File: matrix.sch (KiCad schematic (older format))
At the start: 134 parts, among them K0:0 KEYSW, K0:1 KEYSW, K0:2 KEYSW, K0:3 KEYSW, K0:4 KEYSW, K10:0 KEYSW, K10:1 KEYSW, K10:2 KEYSW, K10:3 KEYSW, K10:4 KEYSW, K11:0 KEYSW, K11:1 KEYSW, K11:2 KEYSW, K11:3 KEYSW, K11:4 KEYSW, K12:0 KEYSW, K12:1 KEYSW, K12:2 KEYSW, K12:3 KEYSW, K12:4 KEYSW, K13:0 KEYSW, K13:1 KEYSW, K13:2 KEYSW, K13:3 KEYSW, K13:4 KEYSW, K1:0 KEYSW, K1:1 KEYSW, K1:2 KEYSW, K1:3 KEYSW, K1:4 KEYSW, K2:0 KEYSW, K2:1 KEYSW, K2:2 KEYSW, K2:3 KEYSW, K2:4 KEYSW, K3:0 KEYSW, K3:1 KEYSW, K3:2 KEYSW, K3:3 KEYSW, K3:4 KEYSW, K4:0 KEYSW, K4:1 KEYSW, K4:2 KEYSW, K4:3 KEYSW, K4:4 KEYSW, K5:0 KEYSW, K5:1 KEYSW, K5:2 KEYSW, K5:3 KEYSW, K5:4 KEYSW, K6:0 KEYSW, K6:1 KEYSW, K6:3 KEYSW, K7:0 KEYSW, K7:1 KEYSW, K7:3 KEYSW, K7:4 KEYSW, K8:0 KEYSW, K8:1 KEYSW, K8:2 KEYSW, K8:3 KEYSW, K8:4 KEYSW, K9:0 KEYSW, K9:1 KEYSW, K9:2 KEYSW, K9:3 KEYSW, K9:4 KEYSW

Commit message: Associate components and footprints
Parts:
- D0:0, D0:1, D0:2, D0:3, D0:4, D10:0, D10:1, D10:2, D10:3, D10:4, D11:0, D11:1, D11:2, D11:3, D11:4, D12:0, D12:1, D12:2, D12:3, D12:4, D13:0, D13:1, D13:2, D13:3, D13:4, D1:0, D1:1, D1:2, D1:3, D1:4, D2:0, D2:1, D2:2, D2:3, D2:4, D3:0, D3:1, D3:2, D3:3, D3:4, D4:0, D4:1, D4:2, D4:3, D4:4, D5:0, D5:1, D5:2, D5:3, D5:4, D6:0, D6:1, D6:3, D7:0, D7:1, D7:3, D7:4, D8:0, D8:1, D8:2, D8:3, D8:4, D9:0, D9:1, D9:2, D9:3, D9:4: footprint (none) -> keyboard_parts:D_SOD123_axial
- K0:0, K0:1, K0:2, K0:3, K0:4, K13:0, K13:1, K13:2, K13:3, K13:4, K6:1, K6:3, K7:1, K7:3: footprint (none) -> keebs:Mx_Alps_150
- K10:0, K10:1, K10:2, K10:3, K10:4, K11:0, K11:1, K11:2, K11:3, K11:4, K12:0, K12:1, K12:2, K12:3, K12:4, K1:0, K1:1, K1:2, K1:3, K1:4, K2:0, K2:1, K2:2, K2:3, K2:4, K3:0, K3:1, K3:2, K3:3, K3:4, K4:0, K4:1, K4:2, K4:3, K4:4, K5:0, K5:1, K5:2, K5:3, K6:0, K7:0, K7:4, K8:0, K8:1, K8:2, K8:3, K8:4, K9:0, K9:1, K9:2, K9:3, K9:4: footprint (none) -> keebs:Mx_Alps_100
- K5:4: footprint (none) -> keebs:Mx_Alps_200

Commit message: Revert "Temp #2"
This reverts commit d15dc5ae93d42b7242c0dbe6693181fd858ed452.
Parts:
- D6:1, D6:3, D7:1, D7:3: footprint keyboard_parts:D_SOD123_axial -> keyboard_parts:Mx_Alps_150_VERT
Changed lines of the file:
@@
 F 0 "D6:1" V 4800 3400 60  0000 C CNN
 F 1 "D" V 5100 3400 60  0001 C CNN
-F 2 "keyboard_parts:D_SOD123_axial" H 4950 3450 60  0001 C CNN
+F 2 "keyboard_parts:Mx_Alps_150_VERT" H 4950 3450 60  0001 C CNN
 F 3 "" H 4950 3450 60  0000 C CNN
 	1    4950 3450
@@
 F 0 "D6:3" V 4800 4700 60  0000 C CNN
 F 1 "D" V 5100 4700 60  0001 C CNN
-F 2 "keyboard_parts:D_SOD123_axial" H 4950 4750 60  0001 C CNN
+F 2 "keyboard_parts:Mx_Alps_150_VERT" H 4950 4750 60  0001 C CNN
 F 3 "" H 4950 4750 60  0000 C CNN
 	1    4950 4750
@@
 F 0 "D7:1" V 5850 3400 60  0000 C CNN
 F 1 "D" V 6150 3400 60  0001 C CNN
-F 2 "keyboard_parts:D_SOD123_axial" H 6000 3450 60  0001 C CNN
+F 2 "keyboard_parts:Mx_Alps_150_VERT" H 6000 3450 60  0001 C CNN
 F 3 "" H 6000 3450 60  0000 C CNN
 	1    6000 3450
@@
 F 0 "D7:3" V 5850 4700 60  0000 C CNN
 F 1 "D" V 6150 4700 60  0001 C CNN
-F 2 "keyboard_parts:D_SOD123_axial" H 6000 4750 60  0001 C CNN
+F 2 "keyboard_parts:Mx_Alps_150_VERT" H 6000 4750 60  0001 C CNN
 F 3 "" H 6000 4750 60  0000 C CNN
 	1    6000 4750

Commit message: Key switches laid out
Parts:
- D6:1, D6:3, D7:1, D7:3: footprint keyboard_parts:Mx_Alps_150_VERT -> keebs:Mx_Alps_150
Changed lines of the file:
@@
 F 0 "D6:1" V 4800 3400 60  0000 C CNN
 F 1 "D" V 5100 3400 60  0001 C CNN
-F 2 "keyboard_parts:Mx_Alps_150_VERT" H 4950 3450 60  0001 C CNN
+F 2 "keebs:Mx_Alps_150" H 4950 3450 60  0001 C CNN
 F 3 "" H 4950 3450 60  0000 C CNN
 	1    4950 3450
@@
 F 0 "D6:3" V 4800 4700 60  0000 C CNN
 F 1 "D" V 5100 4700 60  0001 C CNN
-F 2 "keyboard_parts:Mx_Alps_150_VERT" H 4950 4750 60  0001 C CNN
+F 2 "keebs:Mx_Alps_150" H 4950 4750 60  0001 C CNN
 F 3 "" H 4950 4750 60  0000 C CNN
 	1    4950 4750
@@
 F 0 "D7:1" V 5850 3400 60  0000 C CNN
 F 1 "D" V 6150 3400 60  0001 C CNN
-F 2 "keyboard_parts:Mx_Alps_150_VERT" H 6000 3450 60  0001 C CNN
+F 2 "keebs:Mx_Alps_150" H 6000 3450 60  0001 C CNN
 F 3 "" H 6000 3450 60  0000 C CNN
 	1    6000 3450
@@
 F 0 "D7:3" V 5850 4700 60  0000 C CNN
 F 1 "D" V 6150 4700 60  0001 C CNN
-F 2 "keyboard_parts:Mx_Alps_150_VERT" H 6000 4750 60  0001 C CNN
+F 2 "keebs:Mx_Alps_150" H 6000 4750 60  0001 C CNN
 F 3 "" H 6000 4750 60  0000 C CNN
 	1    6000 4750

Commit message: Layout near completion
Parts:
- K0:0, K0:1, K0:2, K0:3, K0:4: footprint keebs:Mx_Alps_150 -> keebs:Mx_Alps_150_R-5deg
- K10:0, K10:1, K10:2, K10:3, K10:4, K11:0, K11:1, K11:2, K11:3, K11:4, K12:0, K12:1, K12:2, K12:3, K12:4, K7:0, K7:4, K8:0, K8:1, K8:2, K8:3, K8:4, K9:0, K9:1, K9:2, K9:3, K9:4: footprint keebs:Mx_Alps_100 -> keebs:Mx_Alps_100_R5deg
- K13:0, K13:1, K13:2, K13:3, K13:4: footprint keebs:Mx_Alps_150 -> keebs:Mx_Alps_150_R5deg
- K1:0, K1:1, K1:2, K1:3, K1:4, K2:0, K2:1, K2:2, K2:3, K2:4, K3:0, K3:1, K3:2, K3:3, K3:4, K4:0, K4:1, K4:2, K4:3, K4:4, K5:0, K5:1, K5:2, K5:3, K6:0: footprint keebs:Mx_Alps_100 -> keebs:Mx_Alps_100_R-5deg

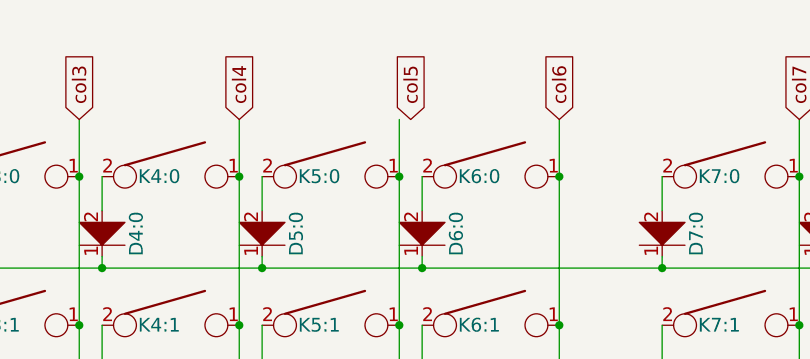
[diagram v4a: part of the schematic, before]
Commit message: More cols wired
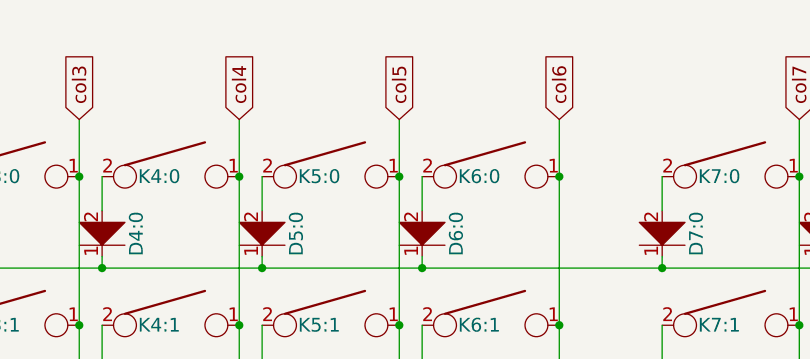
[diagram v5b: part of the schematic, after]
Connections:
- net col5: now also K5:0.1, K5:1.1, K5:2.1, K5:3.1, K5:4.1
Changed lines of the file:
@@
 Text GLabel 4150 2250 1    60   Input ~ 0
 col4
-Text GLabel 4900 2250 1    60   Input ~ 0
+Text GLabel 4850 2250 1    60   Input ~ 0
 col5
 Text GLabel 5550 2250 1    60   Input ~ 0

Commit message: Modify schematics
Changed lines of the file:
@@
 Connection ~ 1350 5100
 Wire Wire Line
-	1350 2250 1350 5100
-Connection ~ 1350 2500
+	1350 2500 1350 5600
 Wire Wire Line
 	750  3550 10850 3550
@@
 Connection ~ 2050 5100
 Wire Wire Line
-	2050 2250 2050 5100
+	2050 2500 2050 5600
 Connection ~ 2050 2500
 Wire Wire Line
@@
 Connection ~ 2750 5100
 Wire Wire Line
-	2750 2250 2750 5100
+	2750 2500 2750 5600
 Connection ~ 2750 2500
 Wire Wire Line
@@
 Connection ~ 3450 5100
 Wire Wire Line
-	3450 2250 3450 5100
+	3450 2500 3450 5600
 Connection ~ 3450 2500
 Wire Wire Line
@@
 Connection ~ 4150 5100
 Wire Wire Line
-	4150 2250 4150 5100
+	4150 2500 4150 5600
 Connection ~ 4150 2500
 Wire Wire Line
@@
 Connection ~ 4850 5100
 Wire Wire Line
-	4850 2250 4850 5100
+	4850 2500 4850 5600
 Connection ~ 4850 2500
 Wire Wire Line
@@
 Connection ~ 5550 3150
 Wire Wire Line
-	5550 2250 5550 4450
+	5550 2500 5550 5600
 Connection ~ 5550 2500
 Connection ~ 750  2900
@@
 Connection ~ 6600 3150
 Wire Wire Line
-	6600 2250 6600 5100
+	6600 2500 6600 5600
 Connection ~ 6600 2500
 Wire Wire Line
@@
 Connection ~ 7300 5100
 Wire Wire Line
-	7300 2250 7300 5100
+	7300 2500 7300 5600
 Connection ~ 7300 2500
 Wire Wire Line
@@
 Connection ~ 8000 5100
 Wire Wire Line
-	8000 2250 8000 5100
+	8000 2500 8000 5600
 Connection ~ 8000 2500
 Wire Wire Line
@@
 Connection ~ 8700 5100
 Wire Wire Line
-	8700 2250 8700 5100
+	8700 2500 8700 5600
 Connection ~ 8700 2500
 Wire Wire Line
@@
 Connection ~ 9400 5100
 Wire Wire Line
-	9400 2250 9400 5100
+	9400 2500 9400 5600
 Connection ~ 9400 2500
 Wire Wire Line
@@
 Connection ~ 10100 5100
 Wire Wire Line
-	10100 2250 10100 5100
+	10100 2500 10100 5600
 Connection ~ 10100 2500
 Wire Wire Line
@@
 Connection ~ 10800 3800
 Wire Wire Line
-	10800 2250 10800 5100
+	10800 2500 10800 5600
 Connection ~ 10800 2500
 Connection ~ 6000 2900
@@
 Connection ~ 6000 5500
 Connection ~ 5550 4450
-Text GLabel 1350 2250 1    60   Input ~ 0
+Text GLabel 1350 5600 3    60   Input ~ 0
 col0
-Text GLabel 2050 2250 1    60   Input ~ 0
+Text GLabel 2050 5600 3    60   Input ~ 0
 col1
-Text GLabel 2750 2250 1    60   Input ~ 0
+Text GLabel 2750 5600 3    60   Input ~ 0
 col2
-Text GLabel 3450 2250 1    60   Input ~ 0
+Text GLabel 3450 5600 3    60   Input ~ 0
 col3
-Text GLabel 4150 2250 1    60   Input ~ 0
+Text GLabel 4150 5600 3    60   Input ~ 0
 col4
-Text GLabel 4850 2250 1    60   Input ~ 0
+Text GLabel 4850 5600 3    60   Input ~ 0
 col5
-Text GLabel 5550 2250 1    60   Input ~ 0
+Text GLabel 5550 5600 3    60   Input ~ 0
 col6
-Text GLabel 6600 2250 1    60   Input ~ 0
+Text GLabel 6600 5600 3    60   Input ~ 0
 col7
-Text GLabel 7300 2250 1    60   Input ~ 0
+Text GLabel 7300 5600 3    60   Input ~ 0
 col8
-Text GLabel 8000 2250 1    60   Input ~ 0
+Text GLabel 8000 5600 3    60   Input ~ 0
 col9
-Text GLabel 8700 2250 1    60   Input ~ 0
+Text GLabel 8700 5600 3    60   Input ~ 0
 col10
-Text GLabel 9400 2250 1    60   Input ~ 0
+Text GLabel 9400 5600 3    60   Input ~ 0
 col11
-Text GLabel 10100 2250 1    60   Input ~ 0
+Text GLabel 10100 5600 3    60   Input ~ 0
 col12
-Text GLabel 10800 2250 1    60   Input ~ 0
+Text GLabel 10800 5600 3    60   Input ~ 0
 col13
 Text GLabel 10850 2900 2    60   Input ~ 0
